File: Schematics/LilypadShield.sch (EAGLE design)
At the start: 36 parts, among them T1 , T2 

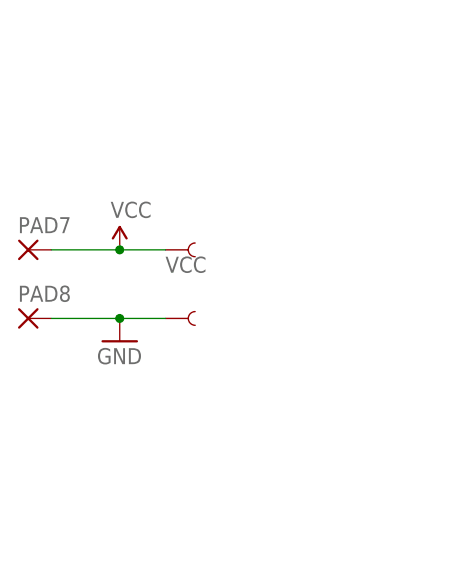
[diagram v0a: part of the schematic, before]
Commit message: New shields and rename
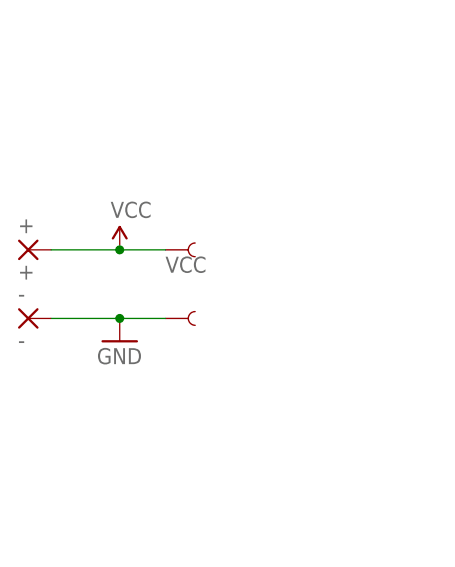
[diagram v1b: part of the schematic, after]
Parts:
- +: value (none) -> +
- -: value (none) -> -
- renumbered PAD7 to +, PAD8 to -
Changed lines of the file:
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@@
 <part name="GND5" library="supply1" deviceset="GND" device=""/>
 <part name="GND6" library="supply1" deviceset="GND" device=""/>
-<part name="PAD7" library="wirepad" deviceset="1,6/0,8" device=""/>
-<part name="PAD8" library="wirepad" deviceset="1,6/0,8" device=""/>
+<part name="+" library="wirepad" deviceset="1,6/0,8" device="" value="+"/>
+<part name="-" library="wirepad" deviceset="1,6/0,8" device="" value="-"/>
 <part name="R1" library="resistor" deviceset="R-EU_" device="0204/5"/>
 <part name="R2" library="resistor" deviceset="R-EU_" device="0204/5"/>
@@
 <instance part="GND5" gate="1" x="78.74" y="147.32"/>
 <instance part="GND6" gate="1" x="170.18" y="149.86"/>
-<instance part="PAD7" gate="P" x="20.32" y="50.8"/>
-<instance part="PAD8" gate="P" x="20.32" y="43.18"/>
+<instance part="+" gate="P" x="20.32" y="50.8"/>
+<instance part="-" gate="P" x="20.32" y="43.18"/>
 <instance part="R1" gate="G$1" x="88.9" y="147.32" rot="R90"/>
 <instance part="R2" gate="G$1" x="66.04" y="147.32" rot="R90"/>
@@
 <pinref part="P+5" gate="1" pin="VCC"/>
 <wire x1="35.56" y1="50.8" x2="30.48" y2="50.8" width="0.1524" layer="91"/>
-<pinref part="PAD7" gate="P" pin="P"/>
+<pinref part="+" gate="P" pin="P"/>
 <wire x1="22.86" y1="50.8" x2="30.48" y2="50.8" width="0.1524" layer="91"/>
 <junction x="30.48" y="50.8"/>
@@
 <pinref part="U$30" gate="G$1" pin="1"/>
 <pinref part="GND1" gate="1" pin="GND"/>
-<pinref part="PAD8" gate="P" pin="P"/>
+<pinref part="-" gate="P" pin="P"/>
 <wire x1="30.48" y1="43.18" x2="22.86" y2="43.18" width="0.1524" layer="91"/>
 <junction x="30.48" y="43.18"/>

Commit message: Fixed board
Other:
- note removed: "LilyPad - MainBoard"
- note removed: "Spark Fun Electronics"
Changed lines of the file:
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@@
 <sheet>
 <plain>
-<text x="154.94" y="27.94" size="3.81" layer="94">LilyPad - MainBoard</text>
-<text x="167.64" y="7.62" size="3.175" layer="94">Spark Fun Electronics</text>
 <text x="158.496" y="93.98" size="1.778" layer="95">/D11</text>
 <text x="158.496" y="91.44" size="1.778" layer="95">/D12</text>

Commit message: Limiting resistors
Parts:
- added R3, R4: (no value), resistor:R-EU_0204/5
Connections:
- new net N$6: LED1.A, R3.1
- new net N$7: LED2.A, R4.1
- net VCC: now also R3.2, R4.2; no longer LED1.A, LED2.A
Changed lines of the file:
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@@
 <?xml version="1.0" encoding="utf-8"?>
 <!DOCTYPE eagle SYSTEM "eagle.dtd">
-<eagle version="6.4">
+<eagle version="6.5.0">
 <drawing>
 <settings>
@@
 <part name="LED1" library="led" deviceset="LED" device="5MM"/>
 <part name="LED2" library="led" deviceset="LED" device="5MM"/>
-<part name="P+1" library="SparkFun" deviceset="VCC" device=""/>
-<part name="P+2" library="SparkFun" deviceset="VCC" device=""/>
 <part name="PAD1" library="wirepad" deviceset="1,6/0,8" device=""/>
 <part name="PAD2" library="wirepad" deviceset="1,6/0,8" device=""/>
@@
 <part name="R1" library="resistor" deviceset="R-EU_" device="0204/5"/>
 <part name="R2" library="resistor" deviceset="R-EU_" device="0204/5"/>
+<part name="R3" library="resistor" deviceset="R-EU_" device="0204/5"/>
+<part name="P+1" library="SparkFun" deviceset="VCC" device=""/>
+<part name="R4" library="resistor" deviceset="R-EU_" device="0204/5"/>
+<part name="P+2" library="SparkFun" deviceset="VCC" device=""/>
 </parts>
 <sheets>
@@
 <instance part="LED1" gate="G$1" x="78.74" y="165.1"/>
 <instance part="LED2" gate="G$1" x="101.6" y="165.1"/>
-<instance part="P+1" gate="1" x="78.74" y="167.64" smashed="yes">
-<attribute name="VALUE" x="77.724" y="171.196" size="1.778" layer="96"/>
-</instance>
-<instance part="P+2" gate="1" x="101.6" y="167.64" smashed="yes">
-<attribute name="VALUE" x="100.584" y="171.196" size="1.778" layer="96"/>
-</instance>
 <instance part="PAD1" gate="P" x="86.36" y="111.76"/>
 <instance part="PAD2" gate="P" x="86.36" y="104.14"/>
@@
 <instance part="R1" gate="G$1" x="88.9" y="147.32" rot="R90"/>
 <instance part="R2" gate="G$1" x="66.04" y="147.32" rot="R90"/>
+<instance part="R3" gate="G$1" x="78.74" y="172.72" rot="R90"/>
+<instance part="P+1" gate="1" x="78.74" y="177.8" smashed="yes">
+<attribute name="VALUE" x="77.724" y="181.356" size="1.778" layer="96"/>
+</instance>
+<instance part="R4" gate="G$1" x="101.6" y="172.72" rot="R90"/>
+<instance part="P+2" gate="1" x="101.6" y="177.8" smashed="yes">
+<attribute name="VALUE" x="100.584" y="181.356" size="1.778" layer="96"/>
+</instance>
 </instances>
 <busses>
@@
 </segment>
 <segment>
-<pinref part="LED1" gate="G$1" pin="A"/>
+<pinref part="R3" gate="G$1" pin="2"/>
 <pinref part="P+1" gate="1" pin="VCC"/>
 </segment>
 <segment>
-<pinref part="LED2" gate="G$1" pin="A"/>
+<pinref part="R4" gate="G$1" pin="2"/>
 <pinref part="P+2" gate="1" pin="VCC"/>
 </segment>
@@
 </segment>
 </net>
+<net name="N$6" class="0">
+<segment>
+<pinref part="LED1" gate="G$1" pin="A"/>
+<pinref part="R3" gate="G$1" pin="1"/>
+</segment>
+</net>
+<net name="N$7" class="0">
+<segment>
+<pinref part="LED2" gate="G$1" pin="A"/>
+<pinref part="R4" gate="G$1" pin="1"/>
+</segment>
+</net>

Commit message: NanoShield
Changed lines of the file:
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@@
+</segment>
+</net>
+<net name="N$8" class="0">
+<segment>
+<wire x1="101.6" y1="160.02" x2="101.6" y2="162.56" width="0.1524" layer="91"/>
 </segment>
 </net>
